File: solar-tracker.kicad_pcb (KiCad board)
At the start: 2 copper layers, 135.9 x 47 mm, 28 parts, among them J1 LDR1, J2 LDR2, J3 Motor, J4 Power_9V, J5 FWD_Limit, J6 REV_Limit, Q1 TIP41C, Q2 TIP41C, Q3 TIP42C, Q4 TIP42C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

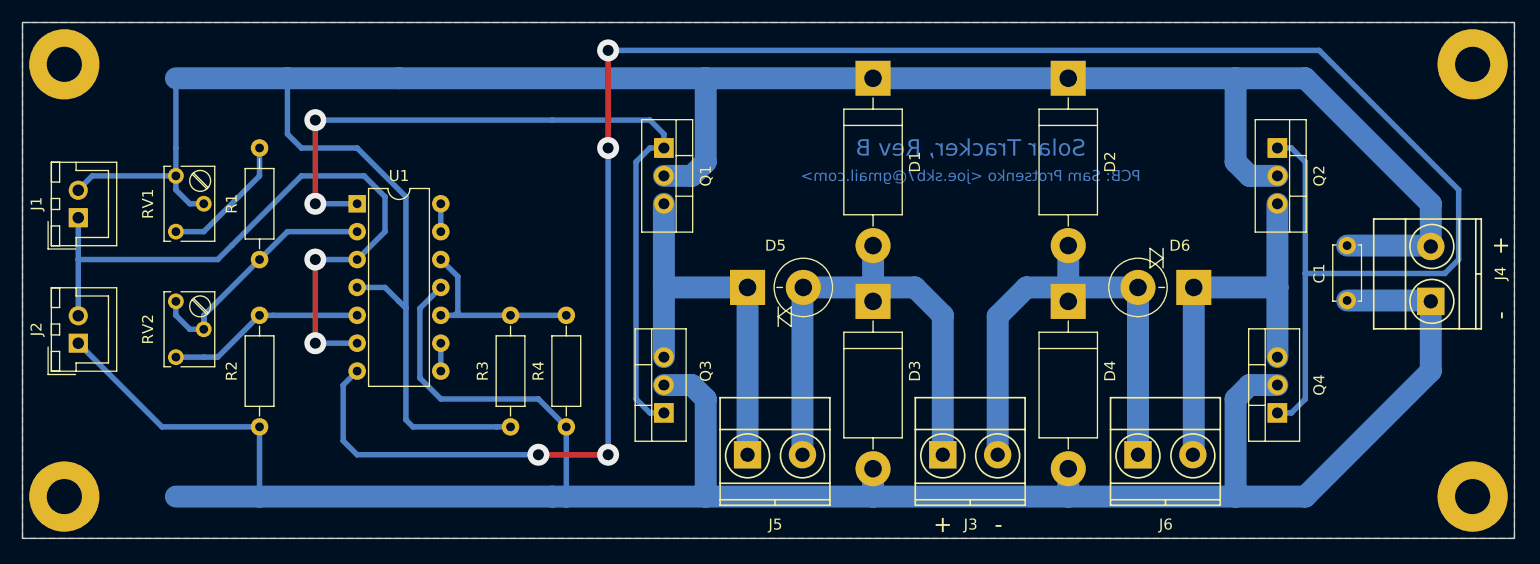
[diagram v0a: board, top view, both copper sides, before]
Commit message: pcb: Route PCB after adding R10, R11
Route new circuit correspondingly.

Signed-off-by: Sam Protsenko <joe.skb7@gmail.com>
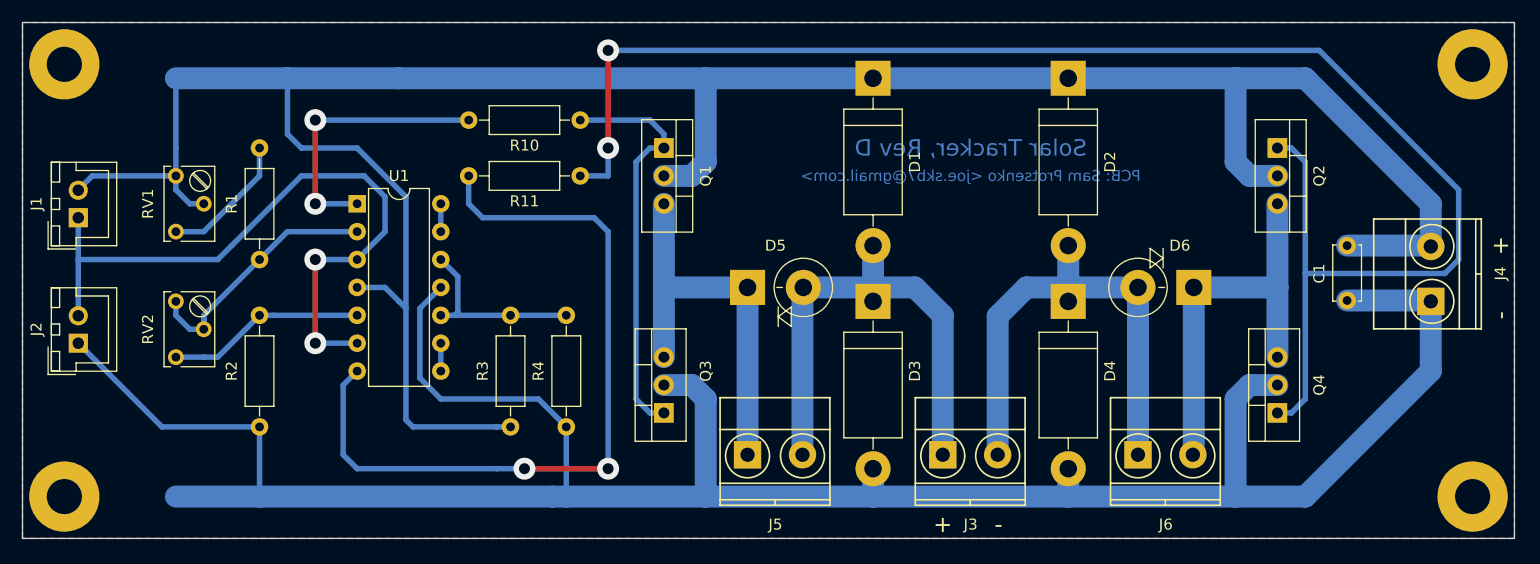
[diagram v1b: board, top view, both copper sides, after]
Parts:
- added R10: 0R, Resistors_THT:R_Axial_DIN0207_L6.3mm_D2.5mm_P10.16mm_Horizontal, F.Cu at (76.2, 34.3)
- added R11: 0R, Resistors_THT:R_Axial_DIN0207_L6.3mm_D2.5mm_P10.16mm_Horizontal, F.Cu at (76.2, 39.4)
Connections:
- U1 pad 1: Net-(Q1-Pad1) -> Net-(R10-Pad2)
- U1 pad 7: Net-(Q2-Pad1) -> Net-(R11-Pad2)
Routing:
- net Net-(R11-Pad2): track 0.00 -> 70.7 mm, vias 0 -> 2
- net Net-(Q2-Pad1): track 199.7 -> 145.3 mm, vias 4 -> 2
- net Net-(Q1-Pad1): track 72.7 -> 37.1 mm, vias 2 -> 0
- net Net-(R10-Pad2): track 0.00 -> 25.4 mm, vias 0 -> 2
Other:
- board text added: "Solar Tracker, Rev D"
- board text removed: "Solar Tracker, Rev B"
